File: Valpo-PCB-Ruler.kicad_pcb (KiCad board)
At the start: 2 copper layers, 203.2 x 38.1 mm, 49 parts

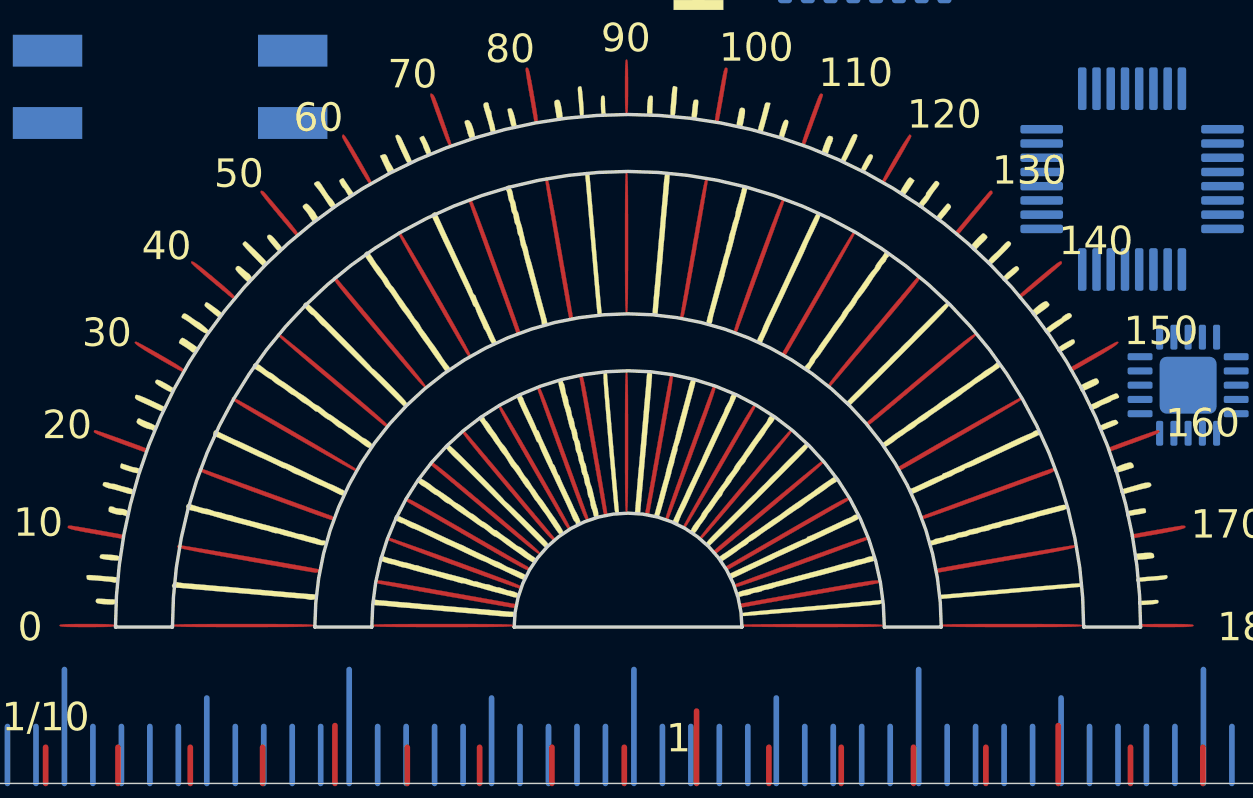
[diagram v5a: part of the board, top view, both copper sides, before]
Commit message: Added lines on back protractor
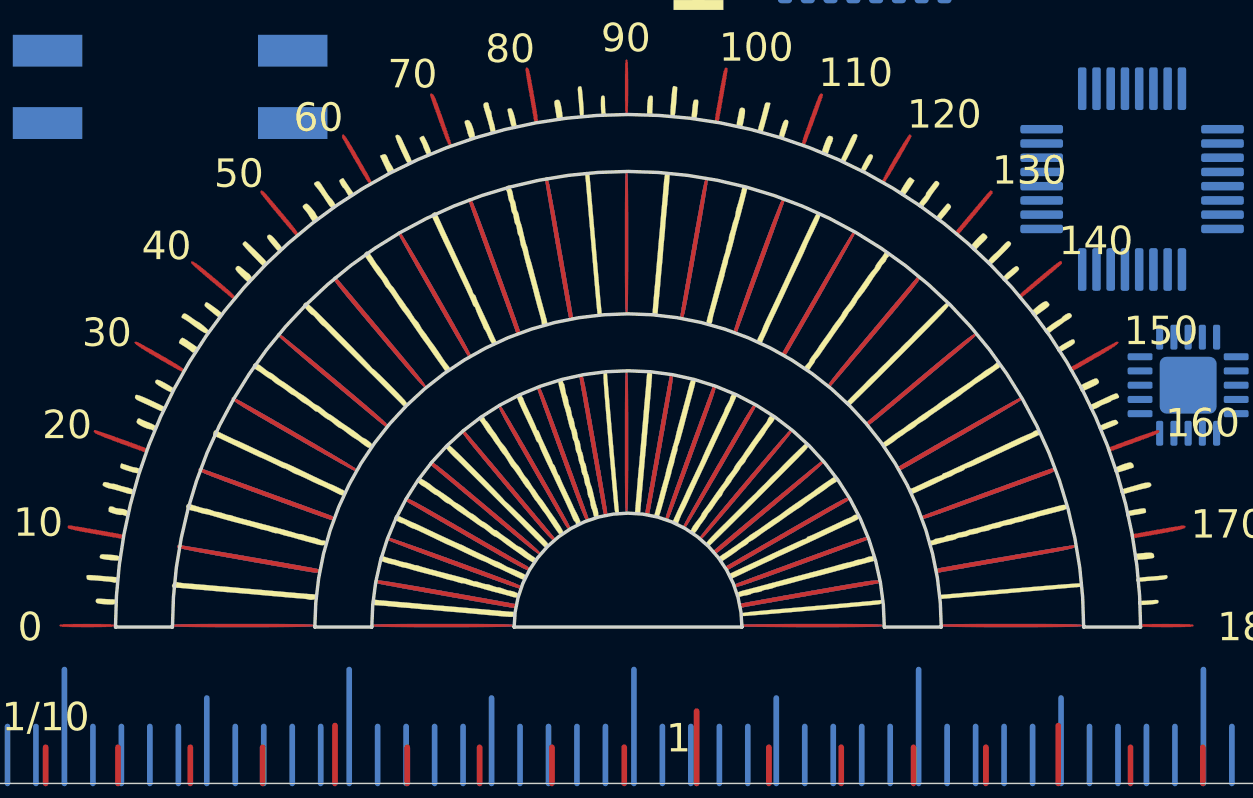
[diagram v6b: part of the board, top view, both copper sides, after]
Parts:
- added G***: LOGO, Valpo-PCB-Ruler-FP:10_Deg_FP, F.Cu at (73.8, 96.1)
- added G***: LOGO, Valpo-PCB-Ruler-FP:Rest_Deg_FP, B.Cu at (73.7, 96.1)
- added G***: LOGO, Valpo-PCB-Ruler-FP:10_Deg_FP, B.Cu at (73.7, 96.1)

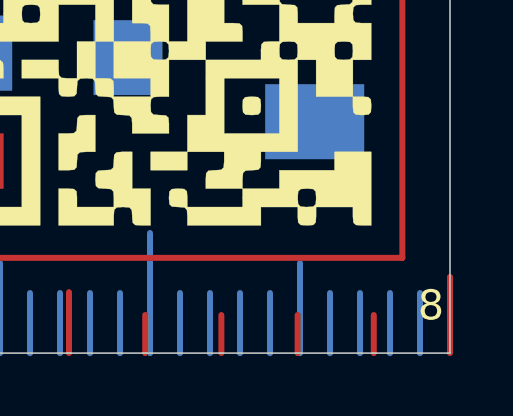
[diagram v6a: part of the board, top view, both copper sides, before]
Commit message: changed RLC to imperial code
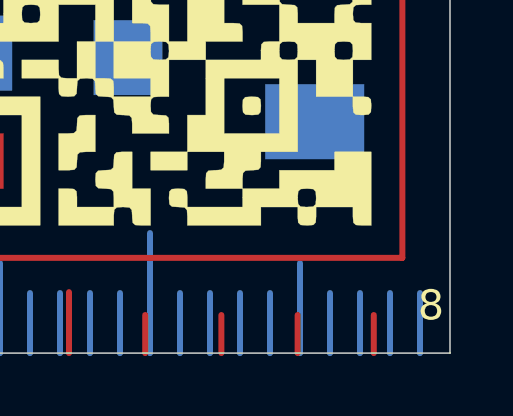
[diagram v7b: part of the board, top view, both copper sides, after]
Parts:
- renumbered 0603 to 0201, 1005 to 0402, 1608 to 0603, 2012 to 0805, 3216 to 1206, 3225 to 1210, 5025 to 2010
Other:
- board text added: "RLC-Imperial"
- board text removed: "RLC-Metric"
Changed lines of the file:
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@@
   (general
     (thickness 1.6)
-    (drawings 1237)
+    (drawings 1235)
     (tracks 20)
     (zones 0)
@@
     (tags resistor)
     (attr smd)
-    (fp_text reference 5025 (at -5.598422 0.09211) (layer B.SilkS)
+    (fp_text reference 2010 (at -5.598422 0.09211) (layer B.SilkS)
       (effects (font (size 1 1) (thickness 0.15)) (justify mirror))
     )
@@
     (tags resistor)
     (attr smd)
-    (fp_text reference 3225 (at -5.098864 0.0265) (layer B.SilkS)
+    (fp_text reference 1210 (at -5.098864 0.0265) (layer B.SilkS)
       (effects (font (size 1 1) (thickness 0.15)) (justify mirror))
     )
@@
     (tags resistor)
     (attr smd)
-    (fp_text reference 3216 (at -4.534364 0) (layer B.SilkS)
+    (fp_text reference 1206 (at -4.534364 0) (layer B.SilkS)
       (effects (font (size 1 1) (thickness 0.15)) (justify mirror))
     )
@@
     (tags resistor)
     (attr smd)
-    (fp_text reference 2012 (at -4.064054 0) (layer B.SilkS)
+    (fp_text reference 0805 (at -4.064054 0) (layer B.SilkS)
       (effects (font (size 1 1) (thickness 0.15)) (justify mirror))
     )
@@
     (tags resistor)
     (attr smd)
-    (fp_text reference 1608 (at -3.81093 0) (layer B.SilkS)
+    (fp_text reference 0603 (at -3.81093 0) (layer B.SilkS)
       (effects (font (size 1 1) (thickness 0.15)) (justify mirror))
     )
@@
     (tags resistor)
     (attr smd)
-    (fp_text reference 1005 (at -3.552182 0.043704) (layer B.SilkS)
+    (fp_text reference 0402 (at -3.552182 0.043704) (layer B.SilkS)
       (effects (font (size 1 1) (thickness 0.15)) (justify mirror))
     )
@@
     (tags resistor)
     (attr smd)
-    (fp_text reference 0603 (at -3.281888 0.03577) (layer B.SilkS)
+    (fp_text reference 0201 (at -3.281888 0.03577) (layer B.SilkS)
       (effects (font (size 1 1) (thickness 0.15)) (justify mirror))
     )
@@
       (xy -4.88682 -4.482967) (xy -4.876452 -4.486047) (xy -4.871357 -4.484994)) (layer F.SilkS) (width 0.01))
   )
+  (gr_line (start 217.554 96.5365) (end 217.554 77.5365) (layer B.SilkS) (width 0.12))
   (gr_text "L=gallons×3.785\n" (at 103.9495 70.9295) (layer B.SilkS)
     (effects (font (size 1 1) (thickness 0.15)) (justify left mirror))
@@
   (gr_line (start 231.14 101.6) (end 231.14 100.33) (layer F.Cu) (width 0.2))
   (gr_line (start 246.38 101.6) (end 246.38 100.33) (layer F.Mask) (width 0.2))
-  (gr_line (start 254 101.6) (end 254 99.06) (layer F.Mask) (width 0.2))
   (gr_line (start 246.38 101.6) (end 246.38 100.33) (layer F.Cu) (width 0.2))
   (gr_line (start 243.84 101.6) (end 243.84 100.33) (layer F.Mask) (width 0.2))
@@
   (gr_line (start 238.76 101.6) (end 238.76 100.33) (layer F.Cu) (width 0.2))
   (gr_line (start 236.22 101.6) (end 236.22 100.33) (layer F.Cu) (width 0.2))
-  (gr_line (start 254 101.6) (end 254 99.06) (layer F.Cu) (width 0.2))
   (gr_line (start 248.92 101.6) (end 248.92 100.33) (layer F.Cu) (width 0.2))
   (gr_line (start 243.84 101.6) (end 243.84 100.33) (layer F.Cu) (width 0.2))
@@
   (gr_line (start 150.0415 65.3265) (end 142.9295 65.3265) (layer B.SilkS) (width 0.12))
   (gr_line (start 176.8385 65.39) (end 168.9645 65.39) (layer B.SilkS) (width 0.12))
-  (gr_line (start 229.5435 79.36) (end 221.098 79.36) (layer B.SilkS) (width 0.12))
+  (gr_line (start 228.464 79.2965) (end 218.2495 79.2965) (layer B.SilkS) (width 0.12))
   (gr_line (start 250.435 80.9475) (end 245.609 80.9475) (layer B.SilkS) (width 0.12))
   (gr_text -6 (at 122.8 78.2805) (layer B.SilkS)
@@
   (gr_arc (start 73.7935 96.108) (end 77.7935 96.108) (angle -180) (layer Edge.Cuts) (width 0.12))
   (gr_line (start 150.8035 64.628) (end 150.8035 88.628) (layer B.SilkS) (width 0.12))
-  (gr_line (start 221 77.6) (end 217 95.6) (layer B.SilkS) (width 0.12))
   (gr_line (start 230 96.6) (end 230 77.6) (layer B.SilkS) (width 0.12))
   (gr_text D2PAK (at 157 76.6) (layer B.SilkS)
@@
     (effects (font (size 1 1) (thickness 0.15)) (justify mirror))
   )
-  (gr_text RLC-Metric (at 225.437 78.643) (layer B.SilkS)
+  (gr_text RLC-Imperial (at 223.5835 78.4225) (layer B.SilkS)
     (effects (font (size 1 1) (thickness 0.15)) (justify mirror))
   )

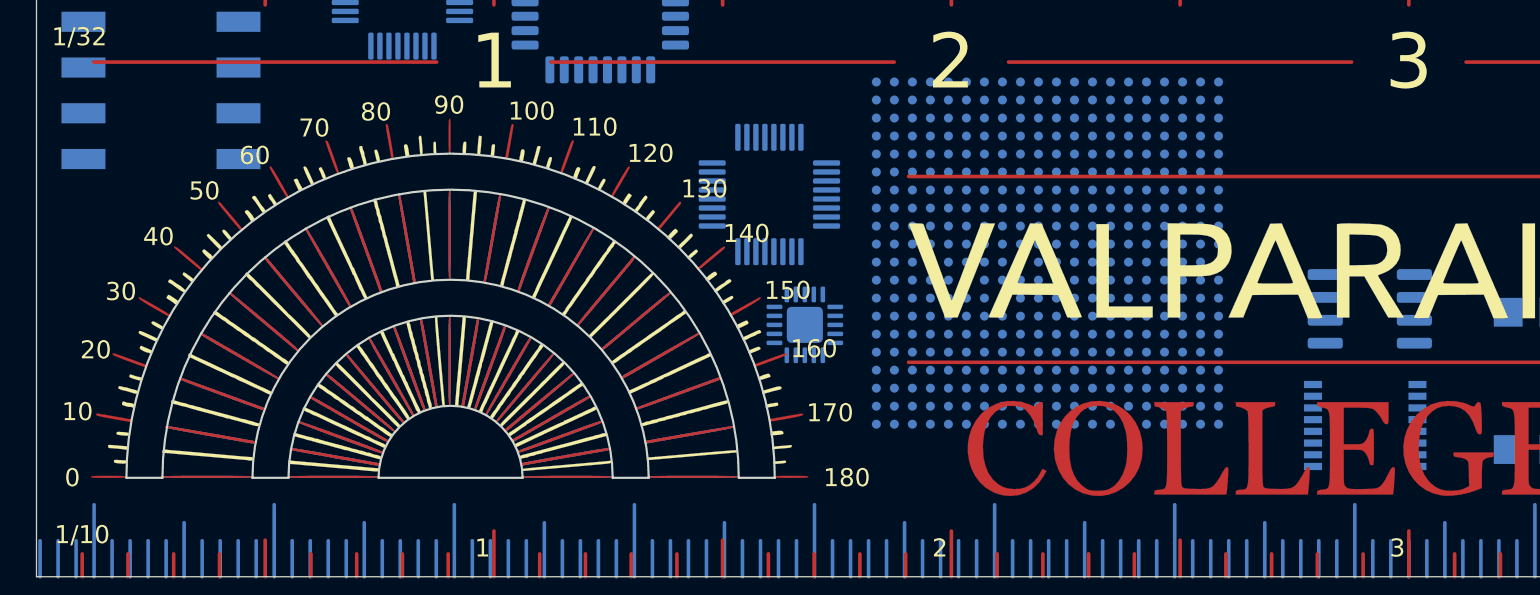
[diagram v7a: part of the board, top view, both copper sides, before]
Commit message: Added Mass Of Electron / Added Designer
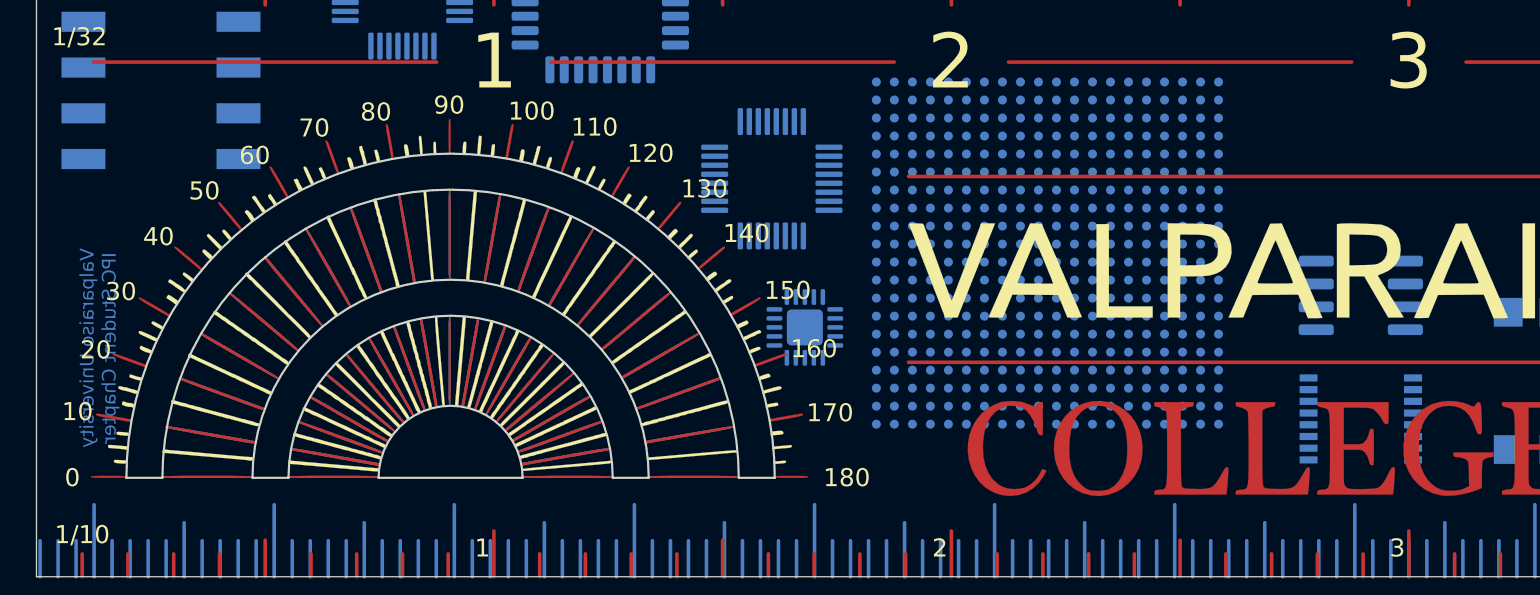
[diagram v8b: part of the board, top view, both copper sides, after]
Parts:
- moved SOIC 0.90 mm to (124.3, 86.0)
- moved QFP 0.88 mm to (91.6, 79.5)
- moved SSOP 0.44 mm to (124.3, 92.8)
- moved QFN 0.14 mm to (93.5, 87.8)
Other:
- board text added: "-31"
- board text added: "Boltzmann Const.(k )= 1.381×10 JK"
- board text added: "Designed By Jacob Leazott"
- board text added: "Electron Volt(eV)=1.602×10 J"
- board text added: "Elementary Charge(q)=1.602×10 C"
- board text added: "Mass of an Electron=9.109×10 kg"
- board text added: "Speed of Light(c)=2.998×10 m/s"
- board text added: "Vacuum Permeability(μ )=1.257×10 H/m"
- board text added: "Vacuum Permittivity(ε )=8.854×10 Fm"
- board text added: "Valparaiso University IPC Student Chapter"
- board text removed: "-2"
- board text removed: "Boltzmann Const.(k )= 1.381x10 JK"
- board text removed: "Coulomb's Const.(k)=8.99×10 Nm C"
- board text removed: "Electron Volt(eV)=1.602x10 J"
- board text removed: "Elementary Charge(q)=1.602*10 C"
- board text removed: "Speed of Light(c)=2.998x10 m/s"
- board text removed: "Vacuum Permeability(μ )=1.257x10 H/m"
- board text removed: "Vacuum Permittivity(ε )=8.854x10 Fm"
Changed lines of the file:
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@@
   (general
     (thickness 1.6)
-    (drawings 1235)
+    (drawings 1236)
     (tracks 20)
     (zones 0)
@@
   )
   (module Package_DFN_QFN:QFN-20-1EP_3.5x3.5mm_P0.5mm_EP2x2mm (layer B.Cu)
-    (at 93.463 87.615)
+    (at 93.463 87.757)
     (descr "QFN, 20 Pin (http://www.ti.com/lit/ml/mpqf239/mpqf239.pdf), generated with kicad-footprint-generator ipc_noLead_generator.py")
     (tags "QFN NoLead")
@@
   )
   (module Package_QFP:LQFP-32_5x5mm_P0.5mm (layer B.Cu)
-    (at 91.4945 80.376)
+    (at 91.6305 79.502)
     (descr "LQFP, 32 Pin (https://www.nxp.com/docs/en/package-information/SOT401-1.pdf), generated with kicad-footprint-generator ipc_gullwing_generator.py")
     (tags "LQFP QFP")
@@
   )
   (module Package_SO:SOIC-8_3.9x4.9mm_P1.27mm (layer B.Cu)
-    (at 124.832 86.726)
+    (at 124.333 85.979)
     (descr "SOIC, 8 Pin (JEDEC MS-012AA, https://www.analog.com/media/en/package-pcb-resources/package/pkg_pdf/soic_narrow-r/r_8.pdf), generated with kicad-footprint-generator ipc_gullwing_generator.py")
     (tags "SOIC SO")
     (attr smd)
-    (fp_text reference SOIC (at 0 0.127 90) (layer B.SilkS)
+    (fp_text reference SOIC (at -0.0675 0.127 90) (layer B.SilkS)
       (effects (font (size 1 1) (thickness 0.15)) (justify mirror))
     )
@@
   )
   (module Package_SO:SSOP-16_4.4x5.2mm_P0.65mm (layer B.Cu)
-    (at 124.578 93.203 180)
+    (at 124.333 92.837 180)
     (descr "SSOP16: plastic shrink small outline package; 16 leads; body width 4.4 mm; (see NXP SSOP-TSSOP-VSO-REFLOW.pdf and sot369-1_po.pdf)")
     (tags "SSOP 0.65")
@@
       (xy -4.88682 -4.482967) (xy -4.876452 -4.486047) (xy -4.871357 -4.484994)) (layer F.SilkS) (width 0.01))
   )
+  (gr_text -31 (at 125.73 78.2955) (layer B.SilkS)
+    (effects (font (size 0.75 0.75) (thickness 0.15)) (justify mirror))
+  )
+  (gr_text "Mass of an Electron=9.109×10  kg" (at 150.122429 79.20847) (layer B.SilkS)
+    (effects (font (size 1 1) (thickness 0.15)) (justify left mirror))
+  )
+  (gr_text "Speed of Sound=343m/s" (at 150.122429 84.2073) (layer B.SilkS)
+    (effects (font (size 1 1) (thickness 0.15)) (justify left mirror))
+  )
+  (gr_text "Valparaiso University\nIPC Student Chapter" (at 54.229 88.9 90) (layer B.Mask)
+    (effects (font (size 0.762 0.762) (thickness 0.127)) (justify mirror))
+  )
+  (gr_text "Valparaiso University\nIPC Student Chapter" (at 54.229 88.9 90) (layer B.Cu)
+    (effects (font (size 0.762 0.762) (thickness 0.127)) (justify mirror))
+  )
+  (gr_text "Designed By Jacob Leazott\n" (at 52.07 89.408 90) (layer B.SilkS)
+    (effects (font (size 0.762 0.762) (thickness 0.127)) (justify mirror))
+  )
   (gr_line (start 217.554 96.5365) (end 217.554 77.5365) (layer B.SilkS) (width 0.12))
   (gr_text "L=gallons×3.785\n" (at 103.9495 70.9295) (layer B.SilkS)
@@
   (gr_line (start 228.464 79.2965) (end 218.2495 79.2965) (layer B.SilkS) (width 0.12))
   (gr_line (start 250.435 80.9475) (end 245.609 80.9475) (layer B.SilkS) (width 0.12))
-  (gr_text -6 (at 122.8 78.2805) (layer B.SilkS)
+  (gr_text -6 (at 122.555 75.692) (layer B.SilkS)
     (effects (font (size 0.75 0.75) (thickness 0.15)) (justify mirror))
   )
-  (gr_text "0\n" (at 133.5315 77.709) (layer B.SilkS)
+  (gr_text "0\n" (at 133.223 75.1205) (layer B.SilkS)
     (effects (font (size 0.75 0.75) (thickness 0.15)) (justify mirror))
   )
-  (gr_text "0\n" (at 132.2615 80.122) (layer B.SilkS)
+  (gr_text "0\n" (at 132.207 77.597) (layer B.SilkS)
     (effects (font (size 0.75 0.75) (thickness 0.15)) (justify mirror))
   )
-  (gr_text "Vacuum Permeability(μ )=1.257x10 H/m" (at 134.4205 79.233) (layer B.SilkS)
+  (gr_text "Vacuum Permeability(μ )=1.257×10 H/m" (at 134.142667 76.709056) (layer B.SilkS)
     (effects (font (size 1 1) (thickness 0.15)) (justify mirror))
   )
-  (gr_text -1 (at 120.3235 75.804) (layer B.SilkS)
+  (gr_text -1 (at 119.9515 73.279) (layer B.SilkS)
     (effects (font (size 0.75 0.75) (thickness 0.15)) (justify mirror))
   )
-  (gr_text -12 (at 123.6255 75.804) (layer B.SilkS)
+  (gr_text -12 (at 123.19 73.279) (layer B.SilkS)
     (effects (font (size 0.75 0.75) (thickness 0.15)) (justify mirror))
   )
-  (gr_text "Vacuum Permittivity(ε )=8.854x10  Fm" (at 135.182357 76.6976) (layer B.SilkS)
+  (gr_text "Vacuum Permittivity(ε )=8.854×10  Fm" (at 134.904572 74.209642) (layer B.SilkS)
     (effects (font (size 1 1) (thickness 0.15)) (justify mirror))
   )
-  (gr_text -19 (at 128.5785 70.6605) (layer B.SilkS)
+  (gr_text -19 (at 128.143 68.2475) (layer B.SilkS)
     (effects (font (size 0.75 0.75) (thickness 0.15)) (justify mirror))
   )
-  (gr_text "Electron Volt(eV)=1.602x10  J" (at 150.185929 71.6488) (layer B.SilkS)
+  (gr_text "Electron Volt(eV)=1.602×10  J" (at 150.122429 69.210814) (layer B.SilkS)
     (effects (font (size 1 1) (thickness 0.15)) (justify left mirror))
   )
-  (gr_text "Speed of Sound=343m/s" (at 150.185929 84.2708) (layer B.SilkS)
+  (gr_text "Speed of Light(c)=2.998×10 m/s" (at 150.122429 81.707884) (layer B.SilkS)
     (effects (font (size 1 1) (thickness 0.15)) (justify left mirror))
   )
-  (gr_text "Speed of Light(c)=2.998x10 m/s" (at 150.185929 81.7464) (layer B.SilkS)
-    (effects (font (size 1 1) (thickness 0.15)) (justify left mirror))
-  )
-  (gr_text 8 (at 128.1905 80.7499) (layer B.SilkS)
+  (gr_text 8 (at 127.6985 80.8355) (layer B.SilkS)
     (effects (font (size 0.75 0.75) (thickness 0.15)) (justify mirror))
   )
-  (gr_text B (at 134.9412 74.7781) (layer B.SilkS)
+  (gr_text B (at 134.8777 72.3651) (layer B.SilkS)
     (effects (font (size 0.75 0.75) (thickness 0.15)) (justify mirror))
   )
-  (gr_text -1 (at 121.53 73.2005) (layer B.SilkS)
+  (gr_text -1 (at 121.031 70.739) (layer B.SilkS)
     (effects (font (size 0.75 0.75) (thickness 0.15)) (justify mirror))
   )
-  (gr_text "Boltzmann Const.(k )= 1.381x10  JK" (at 150.185929 74.1732) (layer B.SilkS)
+  (gr_text "Boltzmann Const.(k )= 1.381×10  JK" (at 150.122429 71.710228) (layer B.SilkS)
     (effects (font (size 1 1) (thickness 0.15)) (justify left mirror))
   )
-  (gr_text -23 (at 124.5272 73.2005) (layer B.SilkS)
-    (effects (font (size 0.75 0.75) (thickness 0.15)) (justify mirror))
-  )
-  (gr_text -19 (at 125.0225 68.1205) (layer B.SilkS)
-    (effects (font (size 0.75 0.75) (thickness 0.15)) (justify mirror))
-  )
-  (gr_text "Elementary Charge(q)=1.602*10  C" (at 150.185929 69.1244) (layer B.SilkS)
-    (effects (font (size 1 1) (thickness 0.15)) (justify left mirror))
-  )
-  (gr_text -2 (at 121.5935 65.7075) (layer B.SilkS)
-    (effects (font (size 0.75 0.75) (thickness 0.15)) (justify mirror))
-  )
-  (gr_text 2 (at 123.6255 65.7075) (layer B.SilkS)
+  (gr_text -23 (at 124.0155 70.739) (layer B.SilkS)
     (effects (font (size 0.75 0.75) (thickness 0.15)) (justify mirror))
   )
-  (gr_text 9 (at 126.8005 65.7075) (layer B.SilkS)
+  (gr_text -19 (at 124.6505 65.7075) (layer B.SilkS)
     (effects (font (size 0.75 0.75) (thickness 0.15)) (justify mirror))
   )
-  (gr_text "Coulomb's Const.(k)=8.99×10 Nm C" (at 150.185929 66.6) (layer B.SilkS)
+  (gr_text "Elementary Charge(q)=1.602×10  C" (at 150.122429 66.7114) (layer B.SilkS)
     (effects (font (size 1 1) (thickness 0.15)) (justify left mirror))
   )
